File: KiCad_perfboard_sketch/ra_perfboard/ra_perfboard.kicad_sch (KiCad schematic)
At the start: 1 part

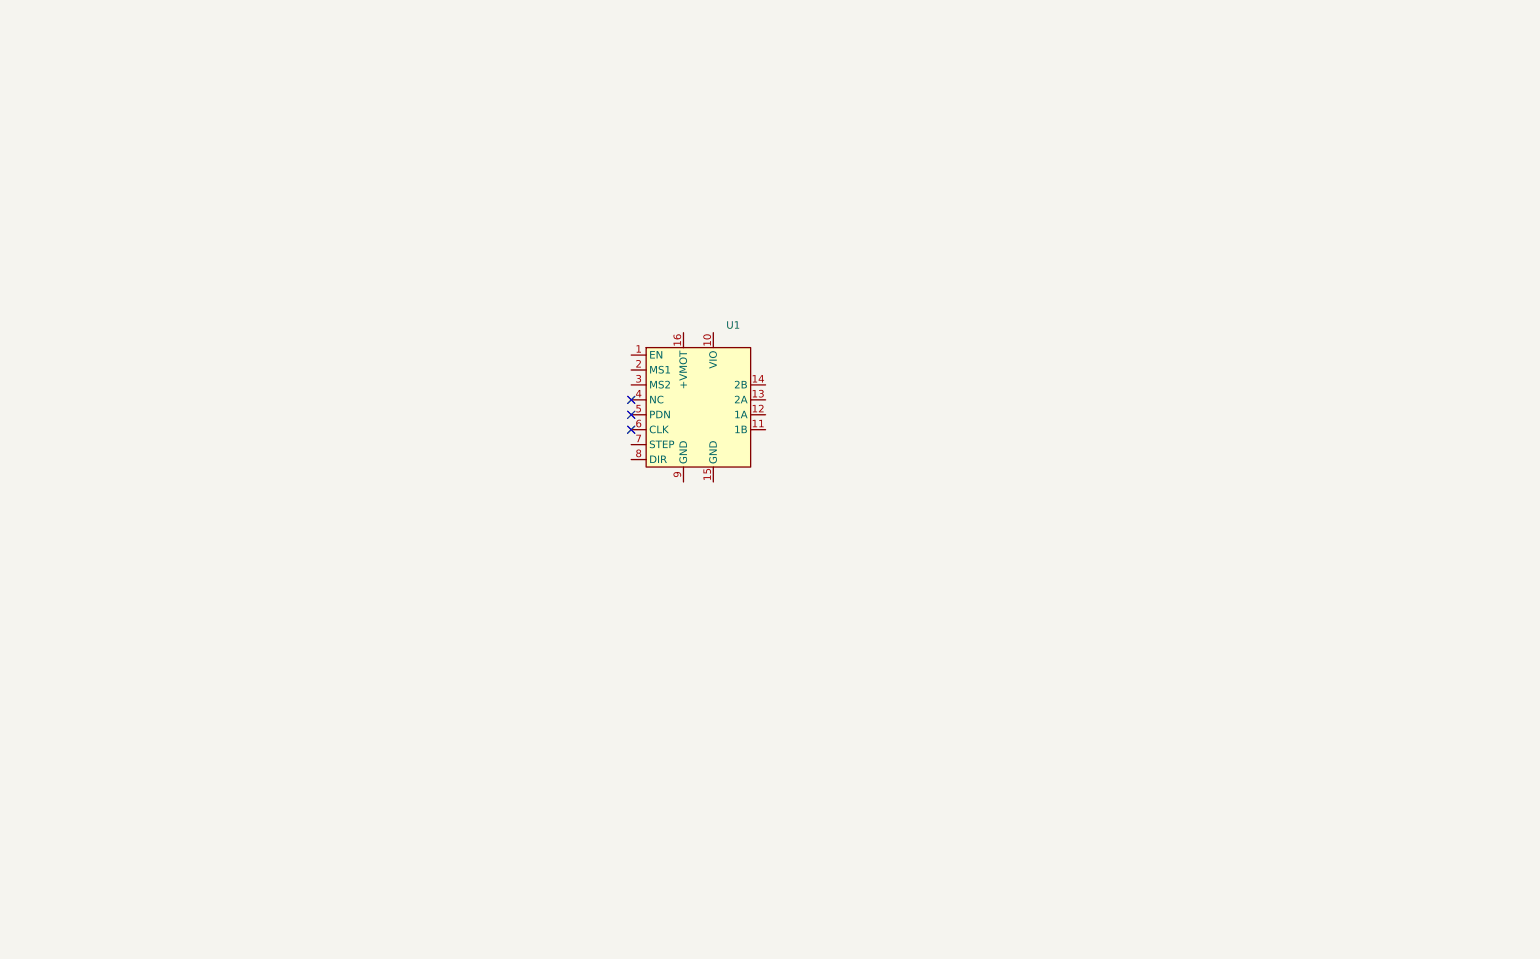
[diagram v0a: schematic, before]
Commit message: Added STM32 board symbol and footprint.
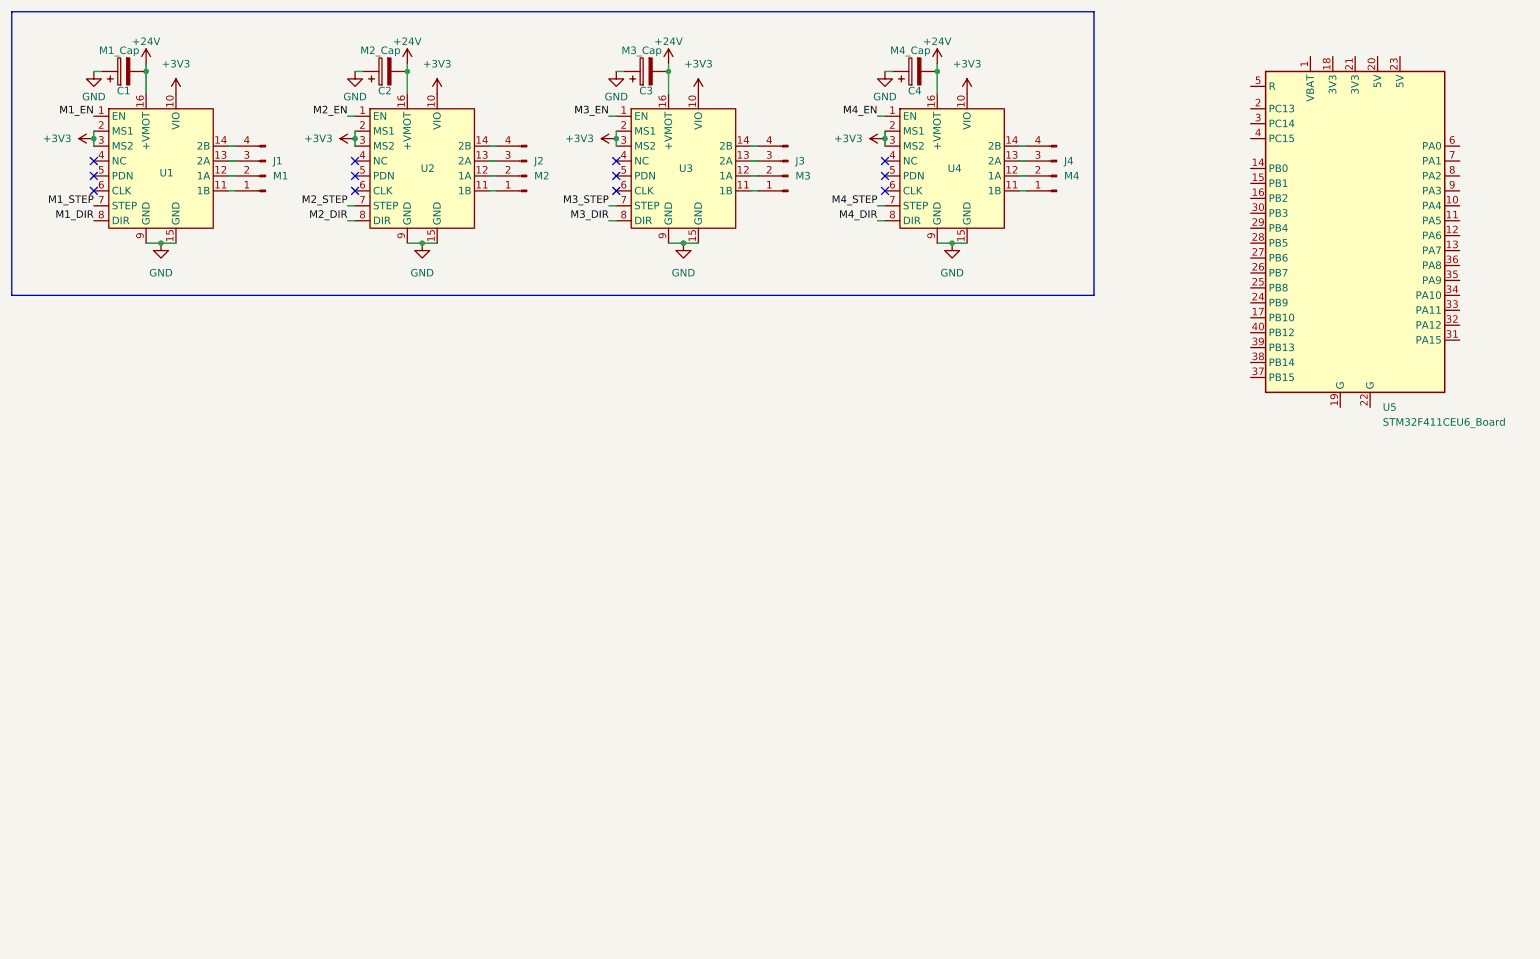
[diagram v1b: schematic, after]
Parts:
- added C1: M1_Cap, Capacitor_THT:CP_Radial_D8.0mm_P3.80mm, symbol Device:C_Polarized
- added C2: M2_Cap, Capacitor_THT:CP_Radial_D8.0mm_P3.80mm, symbol Device:C_Polarized
- added C3: M3_Cap, Capacitor_THT:CP_Radial_D8.0mm_P3.80mm, symbol Device:C_Polarized
- added C4: M4_Cap, Capacitor_THT:CP_Radial_D8.0mm_P3.80mm, symbol Device:C_Polarized
- added J1: M1, Connector_PinHeader_2.54mm:PinHeader_1x04_P2.54mm_Vertical, symbol Connector:Conn_01x04_Pin
- added J2: M2, Connector_PinHeader_2.54mm:PinHeader_1x04_P2.54mm_Vertical, symbol Connector:Conn_01x04_Pin
- added J3: M3, Connector_PinHeader_2.54mm:PinHeader_1x04_P2.54mm_Vertical, symbol Connector:Conn_01x04_Pin
- added J4: M4, Connector_PinHeader_2.54mm:PinHeader_1x04_P2.54mm_Vertical, symbol Connector:Conn_01x04_Pin
- added U2, U3, U4: ~, stm32_ra_board_footprints:TMC2208_Board_Footprint, symbol stm32_ra_boards:TMC2208
- added U5: STM32F411CEU6_Board, stm32_ra_board_footprints:STM32F411CEU6_Board, symbol stm32_ra_boards:STM32F411CEU6_Board
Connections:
- net M1_EN: now reaches U1.1 (EN)
- net +3V3: now reaches U1.10 (VIO)
- net +3V3: now also U1.2 (MS1), U1.3 (MS2), U2.10 (VIO), U2.2 (MS1), U2.3 (MS2), U3.10 (VIO), U3.2 (MS1), U3.3 (MS2), U4.10 (VIO), U4.2 (MS1), U4.3 (MS2)
- net at U1.11 (1B): now also J1.1 (Pin_1)
- net at U1.12 (1A): now also J1.2 (Pin_2)
- net at U1.13 (2A): now also J1.3 (Pin_3)
- net at U1.14 (2B): now also J1.4 (Pin_4)
- net GND: now reaches U1.15 (GND)
- net GND: now also U1.9 (GND), C1.1, C2.1, C3.1, C4.1, U2.15 (GND), U2.9 (GND), U3.15 (GND), U3.9 (GND), U4.15 (GND), U4.9 (GND)
- net +24V: now reaches U1.16 (+VMOT)
- net +24V: now also C1.2, C2.2, C3.2, C4.2, U2.16 (+VMOT), U3.16 (+VMOT), U4.16 (+VMOT)
- net M1_STEP: now reaches U1.7 (STEP)
- net M1_DIR: now reaches U1.8 (DIR)
- new net: J3.1 (Pin_1), U3.11 (1B)
- new net: J3.2 (Pin_2), U3.12 (1A)
- new net: J3.3 (Pin_3), U3.13 (2A)
- new net: J3.4 (Pin_4), U3.14 (2B)
- new net: J4.1 (Pin_1), U4.11 (1B)
- new net: J4.2 (Pin_2), U4.12 (1A)
- new net: J4.3 (Pin_3), U4.13 (2A)
- new net: J4.4 (Pin_4), U4.14 (2B)
- new net: J2.1 (Pin_1), U2.11 (1B)
- new net: J2.2 (Pin_2), U2.12 (1A)
- new net: J2.3 (Pin_3), U2.13 (2A)
- new net: J2.4 (Pin_4), U2.14 (2B)
- new net M2_DIR: U2.8 (DIR)
- new net M2_EN: U2.1 (EN)
- new net M2_STEP: U2.7 (STEP)
- new net M3_DIR: U3.8 (DIR)
- new net M3_EN: U3.1 (EN)
- new net M3_STEP: U3.7 (STEP)
- new net M4_DIR: U4.8 (DIR)
- new net M4_EN: U4.1 (EN)
- new net M4_STEP: U4.7 (STEP)
- no-connect marks 3 -> 12
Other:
- moved on the sheet: U1

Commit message: Added TCA9548A and LM3596 boards to perfboard layout.
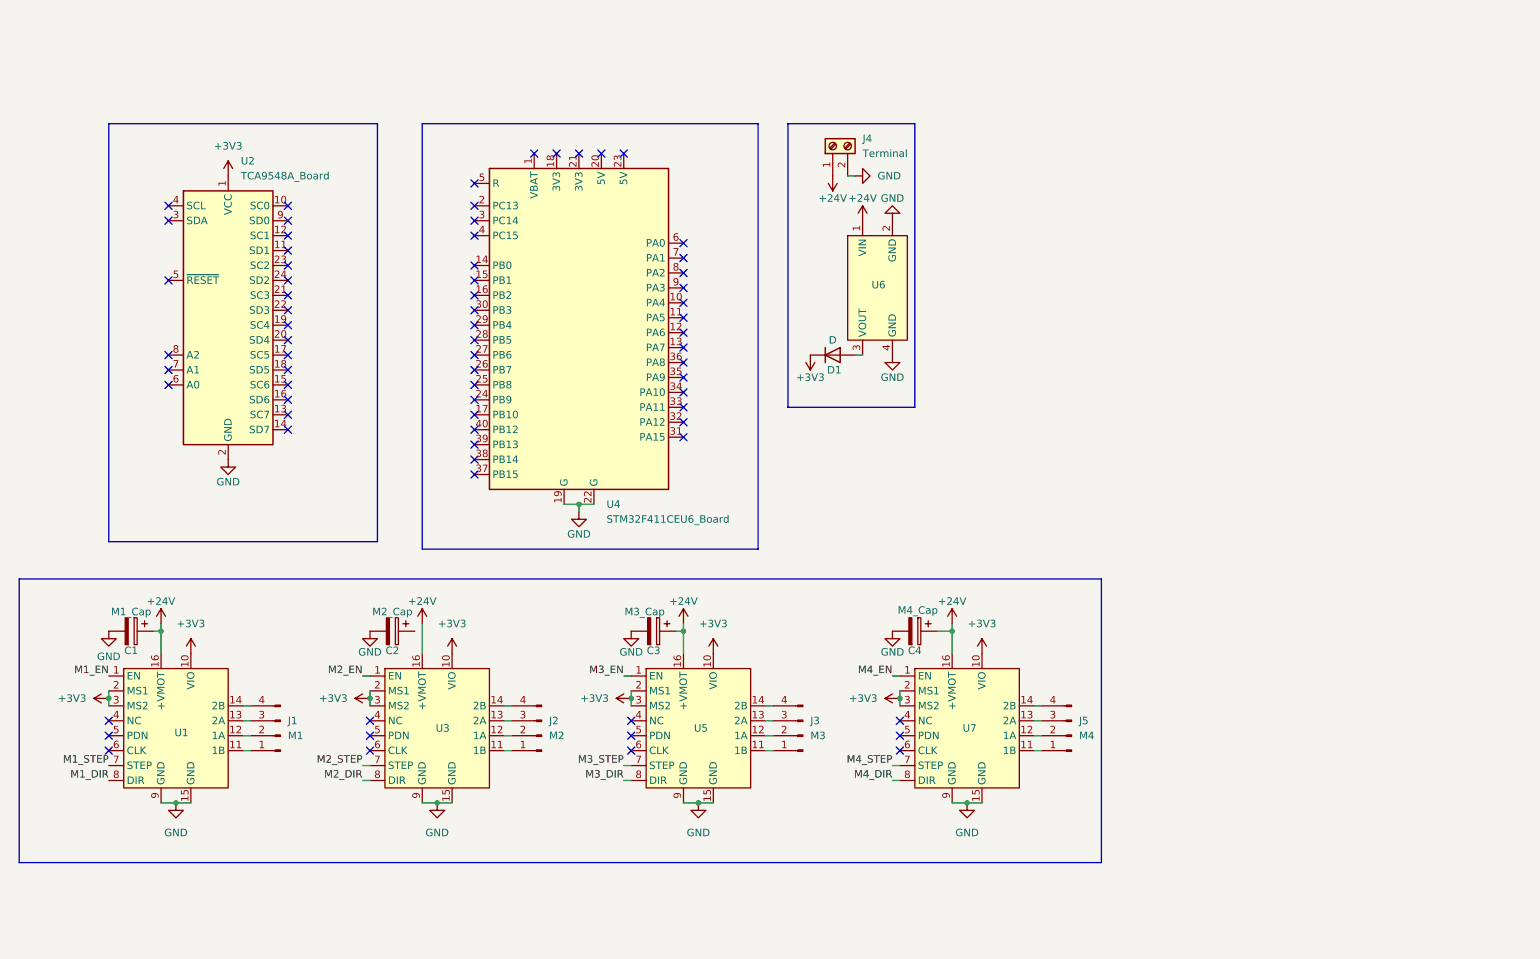
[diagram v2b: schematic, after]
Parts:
- added D1: D, Diode_THT:D_DO-15_P10.16mm_Horizontal, symbol Device:D
- added J4: Terminal, TerminalBlock_Phoenix:TerminalBlock_Phoenix_MKDS-1,5-2-5.08_1x02_P5.08mm_Horizontal, symbol Connector:Screw_Terminal_01x02
- added U2: TCA9548A_Board, stm32_ra_board_footprints:TCA9548A_Board_Footprint, symbol stm32_ra_boards:TCA9548A_Board
- added U6: ~, stm32_ra_board_footprints:LM2596_Board_BC_Footprint, symbol stm32_ra_boards:LM2596_Board_BC
- renumbered J4 to J5, U2 to U3, U5 to U4, U3 to U5, U4 to U7
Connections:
- net +24V: now also C1.1, C3.1, C4.1, J4.1 (Pin_1), U6.1 (VIN); no longer C1.2, C2.2, C3.2, C4.2
- net +3V3: now also D1.1 (K), U2.1 (VCC)
- net GND: now also C1.2, C2.2, C3.2, C4.2, U4.19 (G), U4.22 (G), J4.2 (Pin_2), U2.2 (GND), U6.2 (GND), U6.4 (GND); no longer C1.1, C2.1, C3.1, C4.1
- new net: D1.2 (A), U6.3 (VOUT)
- no-connect marks 12 -> 72
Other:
- moved on the sheet: C1, C2, C3, C4, J1, J2, J3, J5, U1, U3, U4, U5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

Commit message: Configured pins in .ioc file and worked on KiCad perfboard.
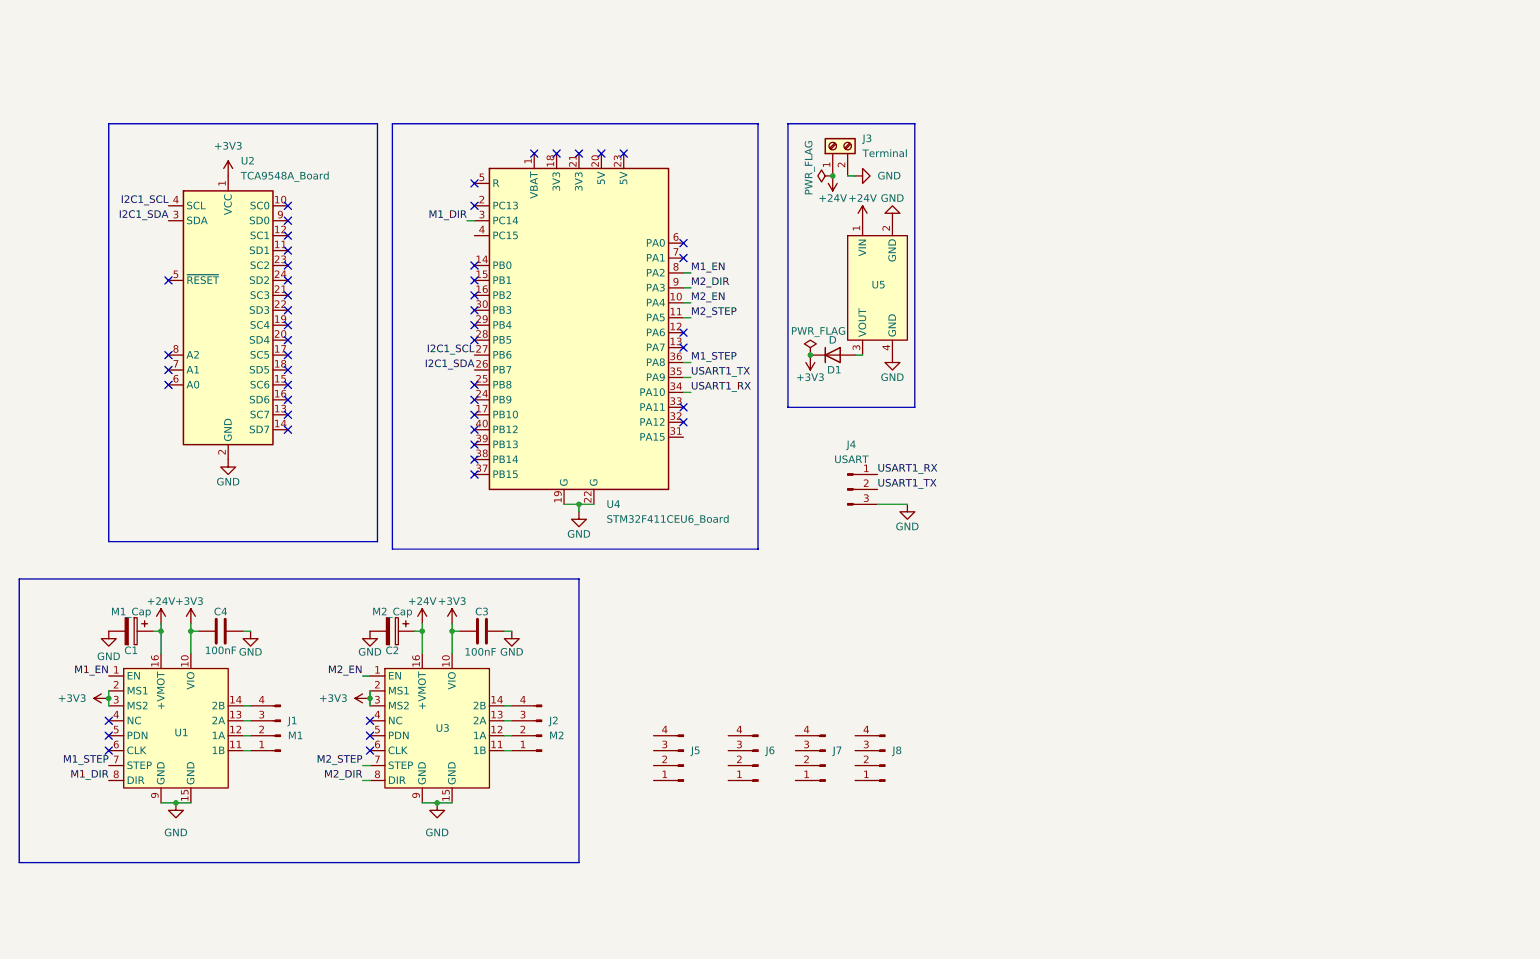
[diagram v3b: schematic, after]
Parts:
- removed C3: M3_Cap, Capacitor_THT:CP_Radial_D8.0mm_P3.80mm, symbol Device:C_Polarized
- removed C4: M4_Cap, Capacitor_THT:CP_Radial_D8.0mm_P3.80mm, symbol Device:C_Polarized
- removed J3: M3, Connector_PinHeader_2.54mm:PinHeader_1x04_P2.54mm_Vertical, symbol Connector:Conn_01x04_Pin
- removed U5, U7: ~, stm32_ra_board_footprints:TMC2208_Board_Footprint, symbol stm32_ra_boards:TMC2208
- added C3: 100nF, symbol Device:C
- added C4: 100nF, Capacitor_THT:C_Disc_D3.0mm_W2.0mm_P2.50mm, symbol Device:C
- added J4: USART, Connector_PinHeader_2.54mm:PinHeader_1x03_P2.54mm_Vertical, symbol Connector:Conn_01x03_Pin
- added J6, J7, J8: ~, Connector_PinHeader_2.54mm:PinHeader_1x04_P2.54mm_Vertical, symbol Connector:Conn_01x04_Pin
- C1, C2: footprint Capacitor_THT:CP_Radial_D8.0mm_P3.80mm -> Capacitor_THT:CP_Radial_D5.0mm_P2.50mm
- J5: value M4 -> ~
- renumbered J4 to J3, U6 to U5
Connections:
- net +24V: now also C2.1
- net +3V3: now also C3.1, C4.1
- net GND: now also C3.2, C4.2, J4.3 (Pin_3)
- net M1_DIR: now also U4.3 (PC14)
- net M1_EN: now also U4.8 (PA2)
- net M1_STEP: now also U4.36 (PA8)
- net M2_DIR: now also U4.9 (PA3)
- net M2_EN: now also U4.10 (PA4)
- net M2_STEP: now also U4.11 (PA5)
- net I2C1_SDA: now reaches U2.3 (SDA)
- net I2C1_SDA: now also U4.26 (PB7)
- net I2C1_SCL: now reaches U2.4 (SCL)
- net I2C1_SCL: now also U4.27 (PB6)
- net USART1_RX: now reaches U4.34 (PA10)
- net USART1_RX: now also J4.1 (Pin_1)
- net USART1_TX: now reaches U4.35 (PA9)
- net USART1_TX: now also J4.2 (Pin_2)
- no-connect marks 72 -> 52

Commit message: Updated commands to be use 2 bytes instead of 1, and made modifications on perfboard and pins.
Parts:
- added J10: L6, Connector_PinHeader_2.54mm:PinHeader_1x04_P2.54mm_Vertical, symbol Connector:Conn_01x04_Pin
- added J9: L5, Connector_PinHeader_2.54mm:PinHeader_1x04_P2.54mm_Vertical, symbol Connector:Conn_01x04_Pin
- C3: footprint (none) -> Capacitor_THT:C_Disc_D3.0mm_W2.0mm_P2.50mm
- J5: value ~ -> L3
- J6: value ~ -> L1
- J7: value ~ -> L2
- J8: value ~ -> L4
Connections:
- net +3V3: now also J5.1 (Pin_1), J6.1 (Pin_1), J7.1 (Pin_1), J8.1 (Pin_1), J10.1 (Pin_1), J9.1 (Pin_1)
- net GND: now also J5.2 (Pin_2), J6.2 (Pin_2), J7.2 (Pin_2), J8.2 (Pin_2), J10.2 (Pin_2), J9.2 (Pin_2)
- net M1_EN: now also U4.4 (PC15); no longer U4.8 (PA2)
- net M1_STEP: now also U4.6 (PA0); no longer U4.36 (PA8)
- net SCL0: now reaches U2.10 (SC0)
- net SCL0: now also J8.4 (Pin_4)
- net SDA1: now reaches U2.11 (SD1)
- net SDA1: now also J5.3 (Pin_3)
- net SCL1: now reaches U2.12 (SC1)
- net SCL1: now also J5.4 (Pin_4)
- net SCL5: now reaches U2.17 (SC5)
- net SCL5: now also J10.4 (Pin_4)
- net SDA5: now reaches U2.18 (SD5)
- net SDA5: now also J10.3 (Pin_3)
- net SCL4: now reaches U2.19 (SC4)
- net SCL4: now also J9.4 (Pin_4)
- net SDA4: now reaches U2.20 (SD4)
- net SDA4: now also J9.3 (Pin_3)
- net SCL3: now reaches U2.21 (SC3)
- net SCL3: now also J6.4 (Pin_4)
- net SDA3: now reaches U2.22 (SD3)
- net SDA3: now also J6.3 (Pin_3)
- net SCL2: now reaches U2.23 (SC2)
- net SCL2: now also J7.4 (Pin_4)
- net SDA2: now reaches U2.24 (SD2)
- net SDA2: now also J7.3 (Pin_3)
- net SDA0: now reaches U2.9 (SD0)
- net SDA0: now also J8.3 (Pin_3)
- no-connect marks 52 -> 38
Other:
- moved on the sheet: J5, J6, J7, J8
